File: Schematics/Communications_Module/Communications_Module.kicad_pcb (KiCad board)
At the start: 2 copper layers, 0 parts

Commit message: Added rough PCB template
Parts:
- added J1: Stack Male Edge Connector, Connector_PCBEdge:BUS_PCIexpress_x1, F.Cu at (66.4, 21.0)
- added J3: SWD_01x04_Pin, SWD_Header:SWD_PinHeader_1x04_P2.54mm_Horizontal, F.Cu at (80.5, 66.2)
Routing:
- added copper zone on In1.Cu, net GND
- added copper zone on In2.Cu, net GND
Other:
- board outline added: 69.5 x 60 mm
- copper layers 2 -> 4

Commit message: Added finalized PCB template
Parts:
- removed J1: Stack Male Edge Connector, Connector_PCBEdge:BUS_PCIexpress_x1
- J3: value SWD_01x04_Pin -> Stack Male Edge Connector; footprint SWD_Header:SWD_PinHeader_1x04_P2.54mm_Horizontal -> Connector_PCBEdge:BUS_PCIexpress_x1
- moved J3 47.3 mm to (66.4, 21.0), turned to 180 degrees
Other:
- board text added: "USE GRID THAT IS SOME MULTIPLE OF 0.1mm (0.1mm, 0.2mm, 0.5mm, 1.0mm, etc)"

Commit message: Power routed?
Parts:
- added AE1: Antenna, footprints:KH-SMA-K513-G, F.Cu at (127.6, 121.7)
- added BZ1: PKM13EPYH4000, footprints:Buzzer_12.6x9.5RM5.0, B.Cu at (123.3, 88.2)
- added C1: 10uF, Capacitor_SMD:C_0603_1608Metric, F.Cu at (154.6, 129.0)
- added C10: 100n, Capacitor_SMD:C_0402_1005Metric, F.Cu at (146.9, 104.8)
- added C11: 0.1uF, Capacitor_SMD:C_0603_1608Metric, F.Cu at (157.7, 106.0)
- added C12: 100n, Capacitor_SMD:C_0402_1005Metric, F.Cu at (137.4, 112.2)
- added C13: 100n, Capacitor_SMD:C_0402_1005Metric, F.Cu at (145.8, 113.3)
- added C14: 10n, Capacitor_SMD:C_0603_1608Metric, F.Cu at (115.8, 89.2)
- added C15: 100nF, Capacitor_SMD:C_0603_1608Metric, F.Cu at (138.9, 101.2)
- added C16: 10p, Capacitor_SMD:C_0603_1608Metric, F.Cu at (146.5, 101.1)
- added C17: 1uF, Capacitor_SMD:CP_Elec_4x5.4, F.Cu at (116.6, 92.9)
- added C18: 10p, Capacitor_SMD:C_0603_1608Metric, F.Cu at (140.5, 101.2)
- added C19: 1uF, Capacitor_SMD:CP_Elec_4x5.4, F.Cu at (117.7, 82.9)
- added C2: 100nF, Capacitor_SMD:C_0603_1608Metric, F.Cu at (147.1, 118.2)
- added C20: 0.1u, Capacitor_SMD:C_0603_1608Metric, F.Cu at (146.7, 91.3)
- added C21: 0.1u, Capacitor_SMD:C_0603_1608Metric, F.Cu at (134.3, 92.8)
- added C3: 10uF, Capacitor_SMD:C_0603_1608Metric, F.Cu at (154.6, 126.7)
- added C4: 1uF, Capacitor_SMD:C_0603_1608Metric, F.Cu at (161.1, 87.1)
- added C5: 1uF, Capacitor_SMD:C_0603_1608Metric, F.Cu at (161.5, 117.4)
- added C6: 1uF, Capacitor_SMD:C_0603_1608Metric, F.Cu at (161.6, 109.3)
- added C7: 100uF, Capacitor_SMD:CP_Elec_6.3x5.9, F.Cu at (160.2, 95.8)
- added C8: 10uF, Capacitor_SMD:CP_Elec_4x5.4, F.Cu at (151.0, 102.4)
- added C9: 100n, Capacitor_SMD:C_0402_1005Metric, F.Cu at (146.4, 103.8)
- added D1: PWR_LED (GRN), LED_SMD:LED_0805_2012Metric, F.Cu at (152.7, 116.4)
- added D2: 1N5819WS, Diode_SMD:D_SOD-323, F.Cu at (123.3, 86.1)
- added D3: 1N5819WS, Diode_SMD:D_SOD-323, F.Cu at (126.8, 86.1)
- added D4: WS2812B, LED_SMD:LED_WS2812B_PLCC4_5.0x5.0mm_P3.2mm, F.Cu at (156.7, 116.1)
- added D5: DB_LED (YLW), LED_SMD:LED_0603_1608Metric, F.Cu at (150.9, 116.5)
- added D6: WS2812B, LED_SMD:LED_WS2812B_PLCC4_5.0x5.0mm_P3.2mm, B.Cu at (156.7, 116.2)
- added FB1: 100R, Resistor_SMD:R_0805_2012Metric, F.Cu at (119.3, 89.2)
- added J1: USB_B_Micro, footprints:USB_Micro-B_Amphenol_10118194_Horizontal, F.Cu at (149.9, 134.6)
- added J2: SWD_01x04_Pin, SWD_Header:SWD_PinHeader_1x04_P2.54mm_Horizontal, F.Cu at (143.4, 126.6)
- added JP1: DIO5_EN, Jumper:SolderJumper-2_P1.3mm_Open_RoundedPad1.0x1.5mm, F.Cu at (133.8, 101.8)
- added Q1: AO3400A, Package_TO_SOT_SMD:SOT-23, F.Cu at (128.8, 91.9)
- added R1: 10k, Resistor_SMD:R_0603_1608Metric, F.Cu at (147.1, 119.7)
- added R10: 10k, Resistor_SMD:R_0603_1608Metric, F.Cu at (128.9, 89.0)
- added R11: 560R, Resistor_SMD:R_0603_1608Metric, F.Cu at (150.9, 113.4)
- added R12: 1k, Resistor_SMD:R_0603_1608Metric, F.Cu at (126.1, 92.0)
- added R13: 30k, Resistor_SMD:R_0603_1608Metric, F.Cu at (157.5, 81.6)
- added R14: 10k, Resistor_SMD:R_0603_1608Metric, F.Cu at (157.5, 84.9)
- added R2: 10k, Resistor_SMD:R_0603_1608Metric, F.Cu at (113.7, 112.6)
- added R3: 10k, Resistor_SMD:R_0603_1608Metric, F.Cu at (134.3, 121.8)
- added R4: 1.5k, Resistor_SMD:R_0603_1608Metric, F.Cu at (151.5, 127.3)
- added R5: 820R, Resistor_SMD:R_0603_1608Metric, F.Cu at (152.7, 113.0)
- added R6: 100k, Resistor_SMD:R_0603_1608Metric, F.Cu at (139.0, 93.9)
- added R7: 10k, Resistor_SMD:R_0603_1608Metric, F.Cu at (154.5, 130.9)
- added R8: 100k, Resistor_SMD:R_0603_1608Metric, F.Cu at (136.0, 110.1)
- added R9: 510R, Resistor_SMD:R_0603_1608Metric, F.Cu at (129.8, 95.7)
- added SW1: SW_STM_RESET, PTS636:PTS636_SK43_SMTR_LFS, F.Cu at (159.8, 132.6)
- added SW2: SW_STM_BOOT_MODE, PTS636:PTS636_SK43_SMTR_LFS, F.Cu at (144.4, 95.8)
- added TP1: TP_VSTACK, TestPoint:TestPoint_Pad_1.5x1.5mm, F.Cu at (162.6, 90.4)
- added TP10: TP_3V3, TestPoint:TestPoint_Pad_1.5x1.5mm, F.Cu at (166.4, 98.9)
- added TP11: TP_BSENSE, TestPoint:TestPoint_Pad_1.5x1.5mm, F.Cu at (162.6, 82.4)
- added TP2: TP_VUSB, TestPoint:TestPoint_Pad_1.5x1.5mm, F.Cu at (163.7, 120.6)
- added TP3: TP_VSWD, TestPoint:TestPoint_Pad_1.5x1.5mm, F.Cu at (146.6, 126.7)
- added TP4: TP_MUX, TestPoint:TestPoint_Pad_1.5x1.5mm, F.Cu at (171.1, 119.8)
- added TP5: TP_PB5, TestPoint:TestPoint_Pad_1.5x1.5mm, F.Cu at (151.0, 109.4)
- added TP6: TP_PB6, TestPoint:TestPoint_Pad_1.5x1.5mm, F.Cu at (154.6, 109.4)
- added TP7: TP_PB7, TestPoint:TestPoint_Pad_1.5x1.5mm, F.Cu at (158.1, 109.4)
- added TP8: TP_ISENSE, TestPoint:TestPoint_Pad_1.5x1.5mm, F.Cu at (184.9, 103.5)
- added TP9: TP_GND, TestPoint:TestPoint_Pad_1.5x1.5mm, F.Cu at (182.6, 85.6)
- added U1: RFM95W-915S2, footprints:RFM95W, F.Cu at (123.3, 108.8)
- added U2: W25Q128JVS, Package_SO:SOIC-8_5.23x5.23mm_P1.27mm, F.Cu at (140.7, 120.3)
- added U3: AMS1117-3.3, Package_TO_SOT_SMD:SOT-223-3_TabPin2, F.Cu at (160.6, 126.7)
- added U4: LM66100DCKR, LMR66100:SC-70-6_Handsoldering, F.Cu at (163.3, 86.7)
- added U5: LM66100DCKR, LMR66100:SC-70-6_Handsoldering, F.Cu at (163.7, 117.0)
- added U6: LM66100DCKR, LMR66100:SC-70-6_Handsoldering, F.Cu at (163.7, 108.9)
- added U7: STM32F103CBT6, Package_QFP:LQFP-48_7x7mm_P0.5mm, F.Cu at (142.2, 108.5)
- added U8: ACS70331EOLC, footprints:SOIC127P600X175-8N, F.Cu at (161.2, 102.5)
- added U9: ISO1042BDWVR, ISO1042:SOIC-8 ISO1042BDWV, F.Cu at (139.0, 88.6)
- added Y1: X322516MMB4SI, Crystal:Crystal_SMD_3225-4Pin_3.2x2.5mm, F.Cu at (143.5, 101.2)
- moved J3 100.1 mm to (148.5, 78.2)
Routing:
- net +3.3V: track 0.00 -> 481.2 mm, vias 0 -> 16
- net V_MUX: track 0.00 -> 125.8 mm
- net V_SWD: track 0.00 -> 48.4 mm, vias 0 -> 2
- net V_BATT: track 0.00 -> 43.4 mm, vias 0 -> 2
- net GND: track 0.00 -> 34.6 mm, vias 0 -> 6
- net +5V: track 0.00 -> 31.5 mm, vias 0 -> 1
- net V_PSU: track 0.00 -> 29.0 mm, vias 0 -> 1
- net V_REGUSB: track 0.00 -> 18.7 mm
- net /USB_5V: track 0.00 -> 16.9 mm
- net BATT_SENSE: track 0.00 -> 6.79 mm
- net Net-(U2-IO2): track 0.00 -> 2.79 mm
- net USB_D+: track 0.00 -> 2.44 mm
- net USB_D-: track 0.00 -> 2.42 mm
- net RESET_RF: track 0.00 -> 2.20 mm
- net RESET_FL: track 0.00 -> 1.93 mm
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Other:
- board text added: "Boot Mode"
- board text added: "Reset"

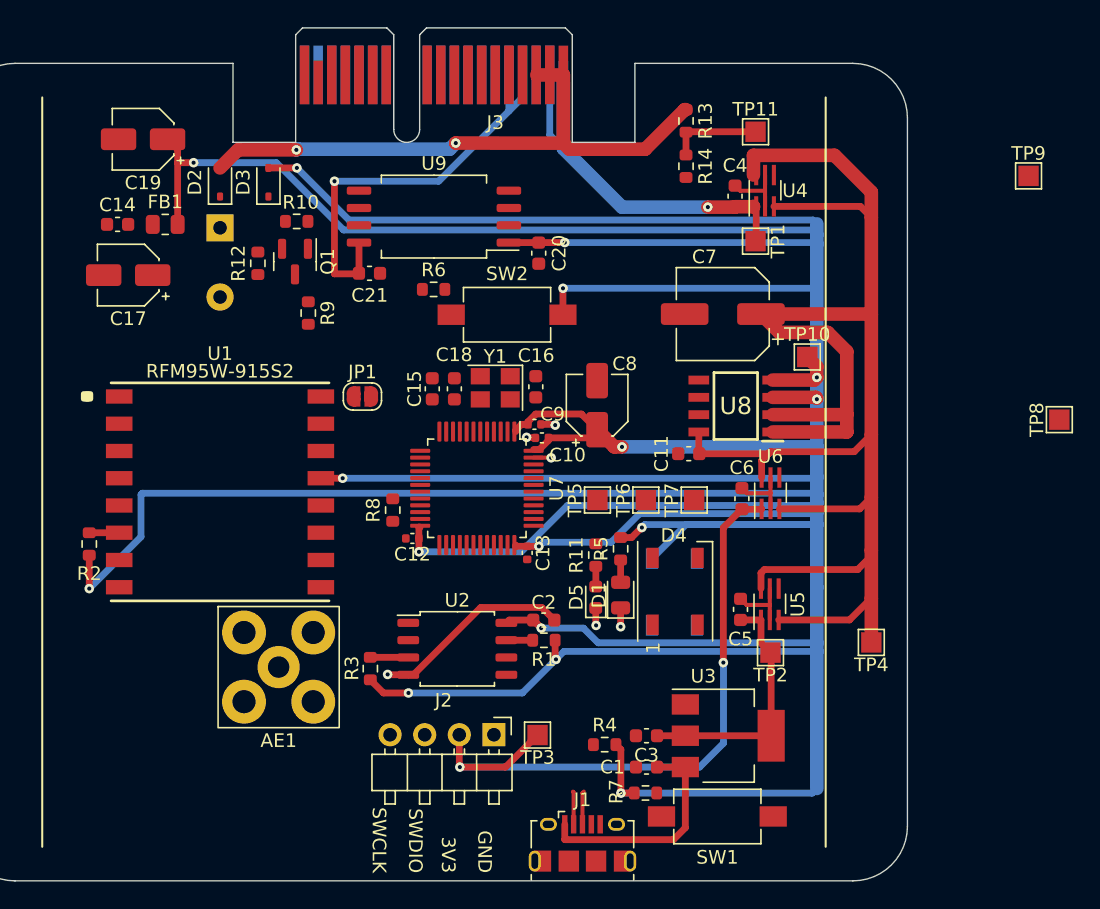
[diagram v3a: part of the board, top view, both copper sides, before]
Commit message: Ground net routed w/ vias
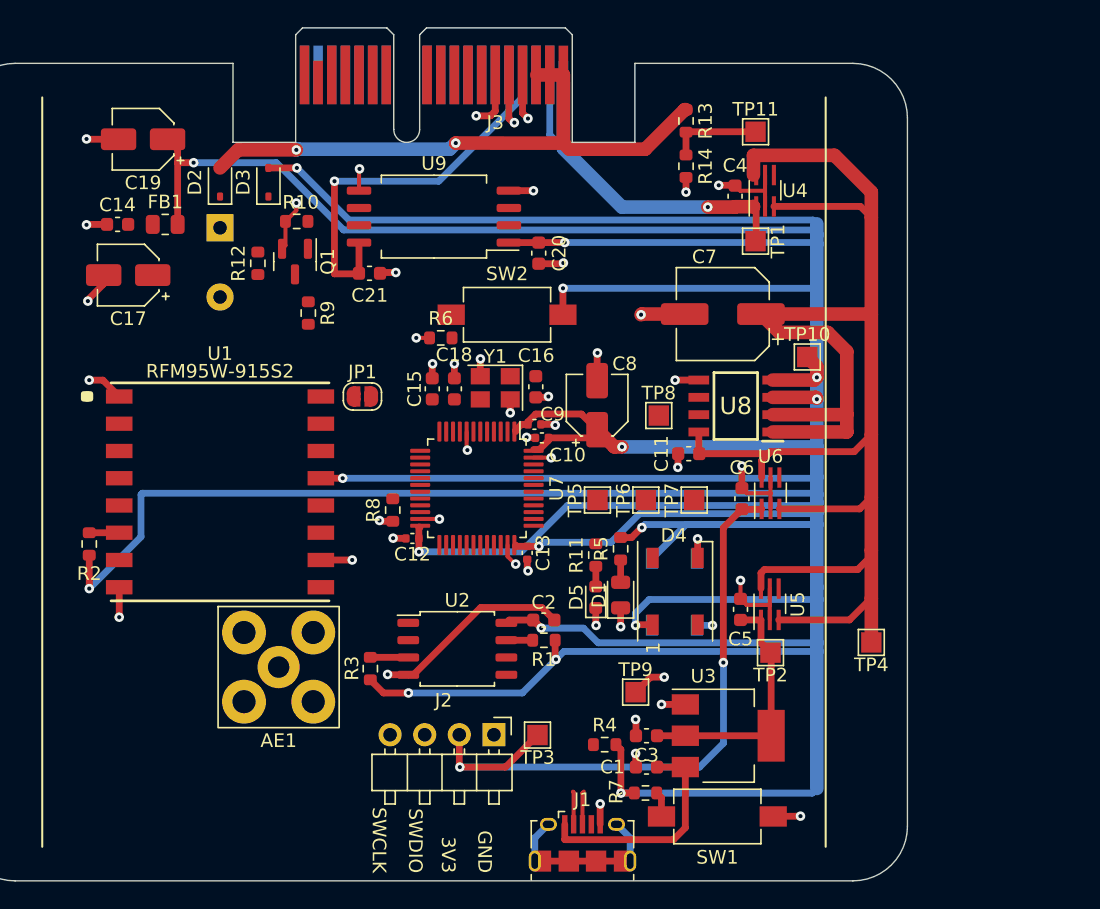
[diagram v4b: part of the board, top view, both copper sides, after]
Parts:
- moved TP9 47.6 mm to (153.8, 123.5)
- moved TP8 29.4 mm to (155.5, 103.2), turned to 0 degrees
- moved R6 3.60 mm to (139.5, 97.5)
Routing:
- net GND: track 34.6 -> 111.4 mm, vias 6 -> 48
- net +3.3V: track 481.2 -> 497.1 mm, vias 16 -> 17
- net unconnected-(J1-Shield-Pad6): track 0.00 -> 13.2 mm
- net STM_RESET: track 0.00 -> 1.87 mm
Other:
- board text added: "-->"
- board text added: "IDK what to do about these ground pins"

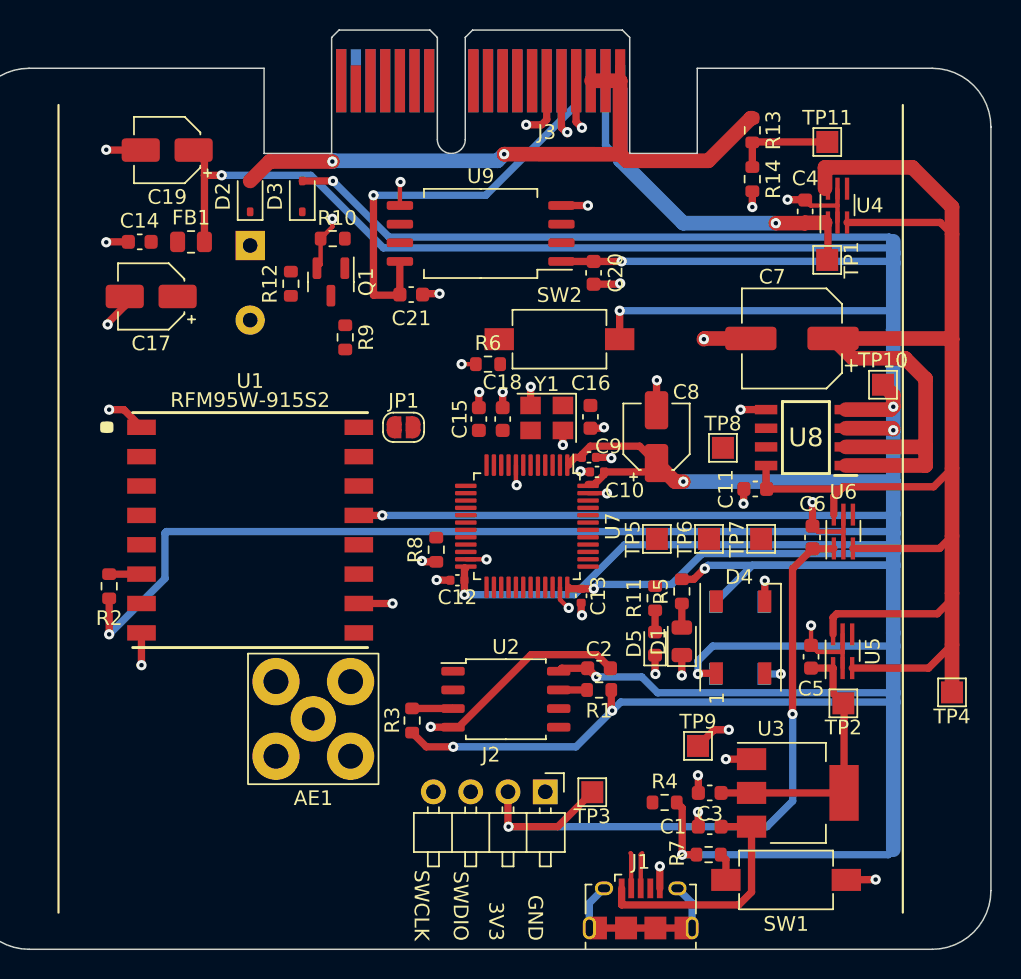
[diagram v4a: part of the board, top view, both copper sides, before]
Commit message: Just a few tough traces left, no antenna yet. 'So close but so far'
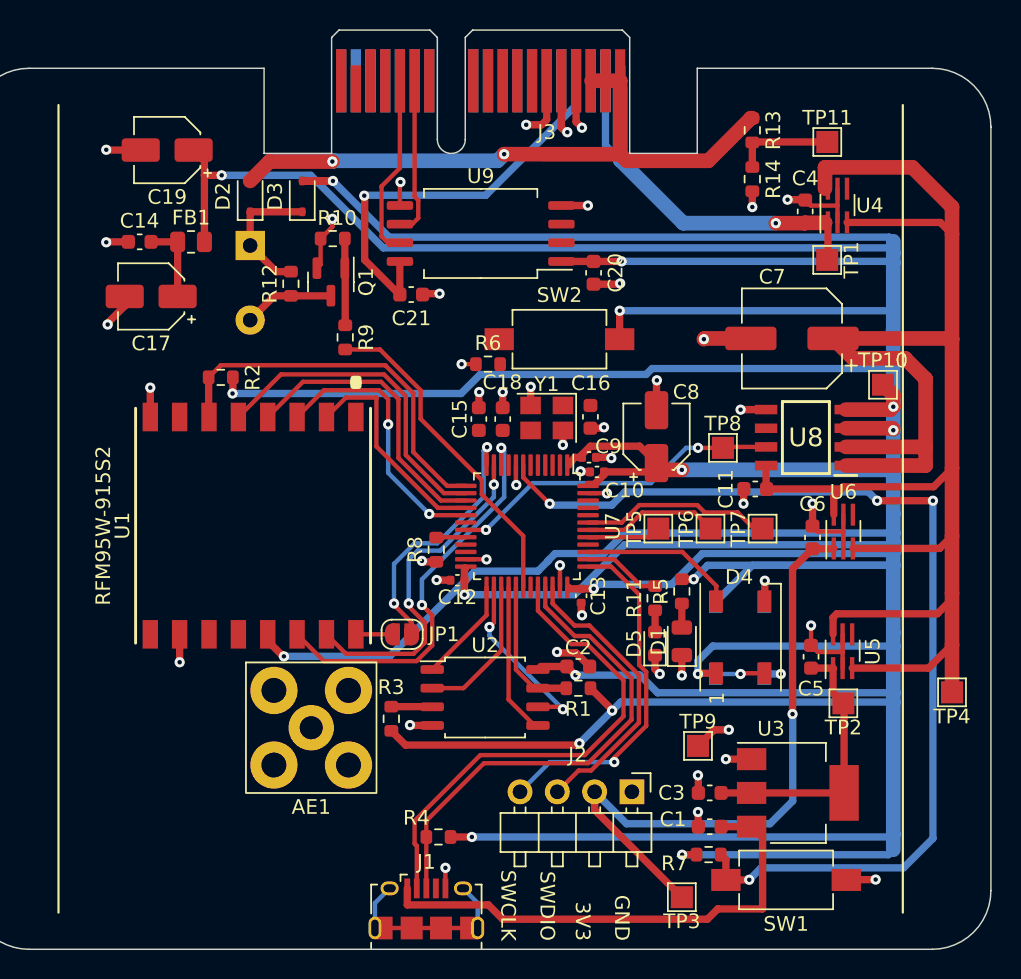
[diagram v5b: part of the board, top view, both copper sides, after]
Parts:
- moved R2 16.1 mm to (121.3, 98.4), turned to 0 degrees
- moved R4 15.6 mm to (136.1, 129.7)
- moved J1 14.6 mm to (135.3, 134.6)
- moved JP1 14.1 mm to (133.7, 115.9)
- moved TP3 9.40 mm to (152.7, 133.8)
- moved J2 5.90 mm to (149.3, 126.6)
- moved R3 1.42 mm to (132.9, 121.7)
- moved R1 1.42 mm to (145.7, 119.6)
- moved C2 1.42 mm to (145.6, 118.1)
- moved U2 1.42 mm to (139.3, 120.2)
- moved TP5 0.71 mm to (151.1, 108.7)
- moved TP6 0.71 mm to (154.7, 108.7)
- moved TP7 0.71 mm to (158.2, 108.7)
- moved AE1 0.62 mm to (127.5, 122.3)
- moved U1 0.36 mm to (123.5, 108.5), turned to -90 degrees
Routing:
- net STM_RESET: track 1.87 -> 70.3 mm, vias 0 -> 4
- net USB_D-: track 2.42 -> 33.7 mm
- net USB_D+: track 2.44 -> 33.5 mm
- net +3.3V: track 497.1 -> 525.5 mm, vias 17 -> 18
- net DIO0_RF: track 0.00 -> 27.7 mm, vias 0 -> 2
- net RESET_RF: track 2.20 -> 26.3 mm
- net SWCLK: track 0.00 -> 24.0 mm, vias 0 -> 1
- net DIO1_RF: track 0.00 -> 23.4 mm, vias 0 -> 2
- net CURR_SENSE: track 0.00 -> 22.8 mm, vias 0 -> 2
- net BUZZER: track 0.00 -> 22.6 mm
- net CS_RF: track 0.00 -> 22.4 mm
- net SCK_RF: track 0.00 -> 20.2 mm
- net SWDIO: track 0.00 -> 19.7 mm
- net MOSI_RF: track 0.00 -> 18.7 mm, vias 0 -> 2
- net DIO2_RF: track 0.00 -> 17.9 mm, vias 0 -> 2
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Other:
- board text added: "Going to be awful: - DB_LED - Batt_sense - 3.3VA"
- board text added: "Gross Trace Tracker (they all are, but here's the worst): - STM Reset - USB Diff Pair? - SCK_FL - Curr_sense - MOSI_RF - RF DIOx traces - Buzzer (PWM right? something should prob be done about that one)"

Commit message: small changes
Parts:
- moved R6 2.48 mm to (137.7, 95.8)
- moved SW2 2.45 mm to (142.6, 94.1)
- moved C18 0.50 mm to (140.5, 100.7)
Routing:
- net GND: track 97.2 -> 109.5 mm, vias 48 -> 51
- net STM_RESET: track 70.3 -> 74.8 mm
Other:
- board text added: "Going to be awful: - DB_LED - Batt_sense - 3.3VA - oscillator"
- board text removed: "Going to be awful: - DB_LED - Batt_sense - 3.3VA"
